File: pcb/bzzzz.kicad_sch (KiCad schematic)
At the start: 13 parts, among them J1 OUT, J2 OUT, Q1 FDD8424H

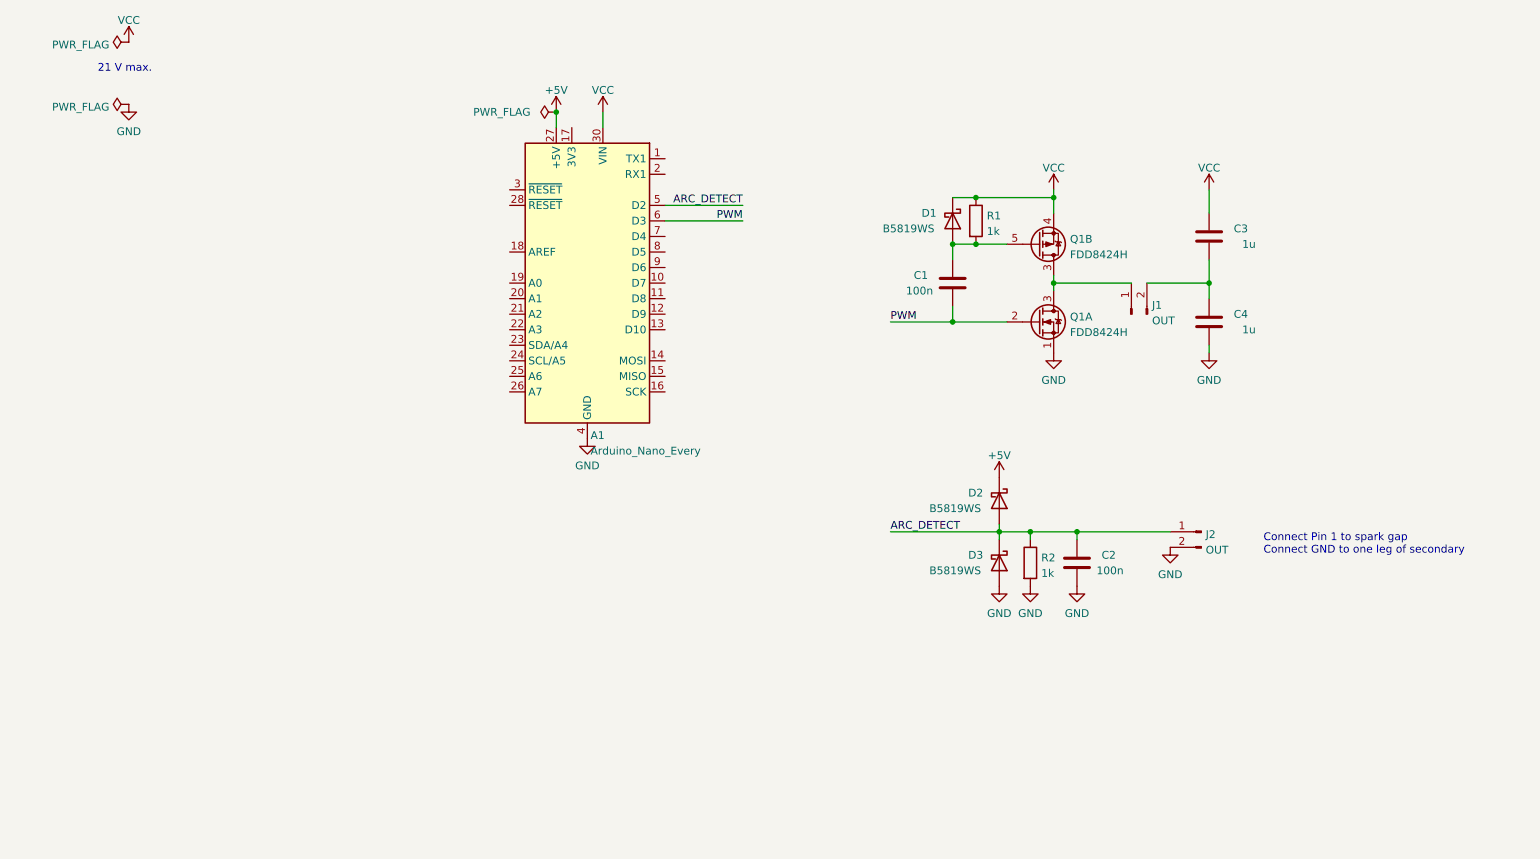
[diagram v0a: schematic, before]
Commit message: pcb: routing finished of a nice symmetric full-bridge
PCB fits below Arduino
Still need to choose smaller connectors
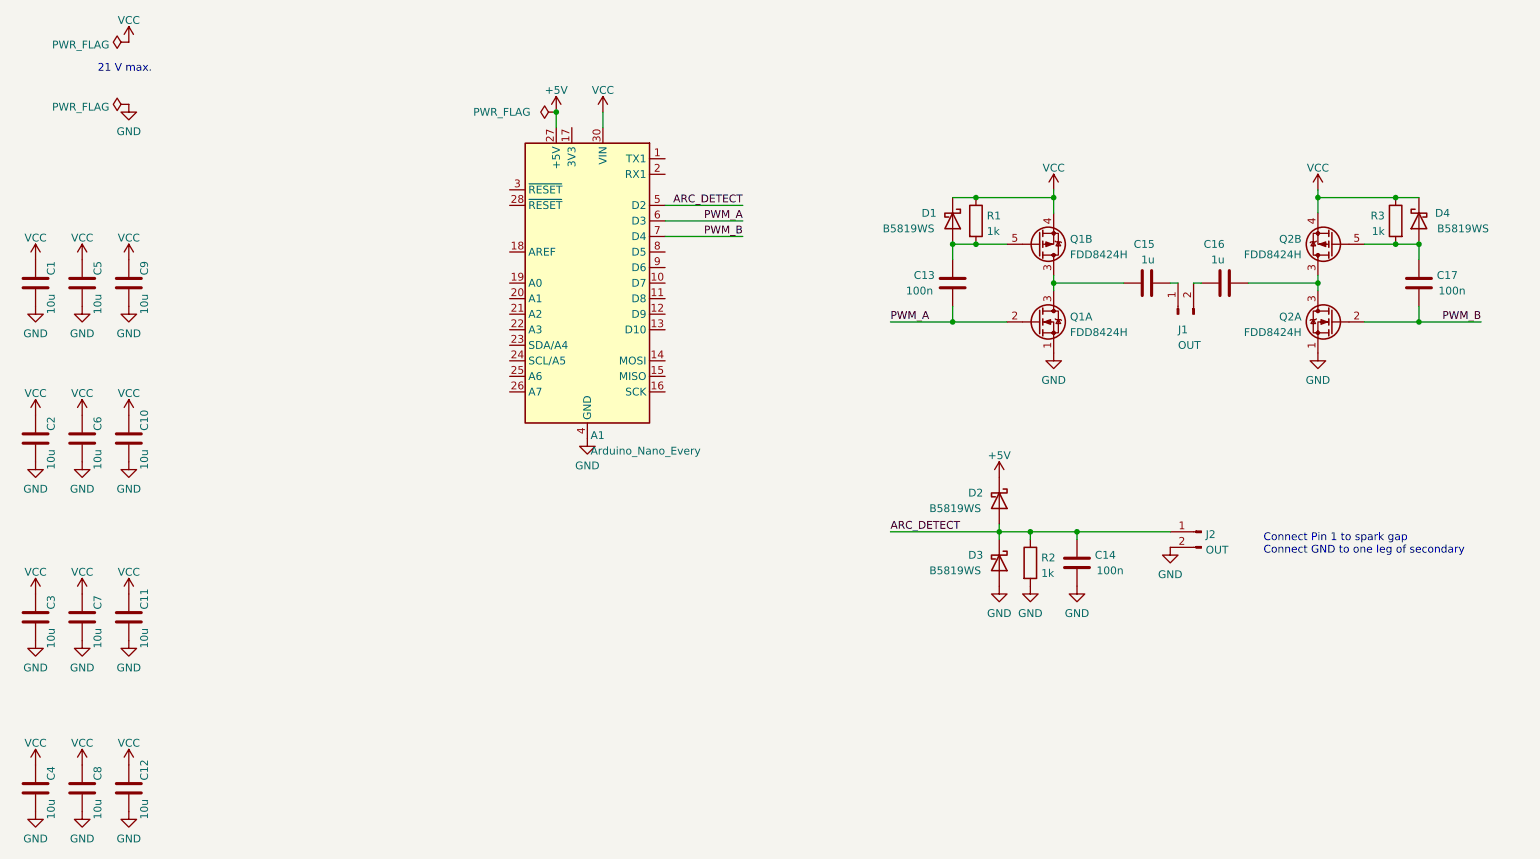
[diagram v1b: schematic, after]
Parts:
- added C1, C10, C11, C12, C2, C3, C5, C6, C7, C8, C9: 10u, Capacitor_SMD:C_0805_2012Metric, symbol Device:C
- added C16: 1u, Capacitor_SMD:C_1812_4532Metric, symbol Device:C
- added C17: 100n, Capacitor_SMD:C_0805_2012Metric, symbol Device:C
- added D4: B5819WS, Diode_SMD:D_SOD-323_HandSoldering, symbol Device:D_Schottky
- added Q2: FDD8424H, Package_TO_SOT_SMD:TO-252-4, symbol bzzzzz:FDD8424H
- added R3: 1k, Resistor_SMD:R_0805_2012Metric, symbol Device:R
- C15: renamed from C3; footprint Capacitor_SMD:C_0805_2012Metric -> Capacitor_SMD:C_1812_4532Metric
- C4: value 1u -> 10u
- renumbered C1 to C13, C2 to C14
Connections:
- net GND: now also C1.2, C10.2, C11.2, C12.2, C2.2, C3.2, C5.2, C6.2, C7.2, C8.2, C9.2, Q2.1 (S)
- net VCC: now also C4.1, C1.1, C10.1, C11.1, C12.1, C2.1, C3.1, C5.1, C6.1, C7.1, C8.1, C9.1, D4.1 (K), Q2.4 (S), R3.1; no longer C15.1
- net at Q1.3 (D), Q1.3 (D): now also C15.1; no longer J1.1 (Pin_1)
- net PWM_B: now reaches A1.7 (D4)
- net PWM_B: now also C17.2, Q2.2 (G)
- net PWM renamed PWM_A
- new net: C15.2, J1.1 (Pin_1)
- new net: C16.1, J1.2 (Pin_2)
- new net: C16.2, Q2.3 (D), Q2.3 (D)
- new net: C17.1, D4.2 (A), Q2.5 (G), R3.2
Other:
- moved on the sheet: C15, J1

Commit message: pcb ordered from jlc
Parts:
- added J1: PWR, Connector_PinHeader_2.54mm:PinHeader_1x02_P2.54mm_Horizontal, symbol Connector:Conn_01x02_Male
- J3: renamed from J2; value OUT -> ARC
- renumbered J1 to J2
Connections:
- net ARC_DETECT: now also A1.11 (D8); no longer A1.5 (D2)
- net GND: now also J1.2 (Pin_2)
- net PWM_A: now also A1.9 (D6); no longer A1.6 (D3)
- net PWM_B: now also A1.12 (D9); no longer A1.7 (D4)
- net VCC: now also J1.1 (Pin_1)
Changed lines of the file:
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@@
   (junction (at 194.31 124.46) (diameter 0) (color 0 0 0 0)
   )
+  (junction (at 52.07 54.61) (diameter 0) (color 0 0 0 0)
+  )
+  (junction (at 52.07 44.45) (diameter 0) (color 0 0 0 0)
+  )
   (junction (at 207.01 124.46) (diameter 0) (color 0 0 0 0)
   )
@@
     (stroke (width 0) (type default) (color 0 0 0 0))
   )
-  (wire (pts (xy 139.7 76.2) (xy 152.4 76.2))
+  (wire (pts (xy 139.7 88.9) (xy 152.4 88.9))
     (stroke (width 0) (type default) (color 0 0 0 0))
   )
@@
     (stroke (width 0) (type default) (color 0 0 0 0))
   )
+  (wire (pts (xy 52.07 50.8) (xy 52.07 54.61))
+    (stroke (width 0) (type default) (color 0 0 0 0))
+  )
   (wire (pts (xy 199.39 124.46) (xy 207.01 124.46))
     (stroke (width 0) (type default) (color 0 0 0 0))
@@
     (stroke (width 0) (type default) (color 0 0 0 0))
   )
+  (wire (pts (xy 52.07 44.45) (xy 52.07 48.26))
+    (stroke (width 0) (type default) (color 0 0 0 0))
+  )
   (wire (pts (xy 246.38 83.82) (xy 246.38 85.09))
     (stroke (width 0) (type default) (color 0 0 0 0))
@@
     (stroke (width 0) (type default) (color 0 0 0 0))
   )
-  (wire (pts (xy 152.4 71.12) (xy 139.7 71.12))
+  (wire (pts (xy 152.4 86.36) (xy 139.7 86.36))
     (stroke (width 0) (type default) (color 0 0 0 0))
   )
@@
     (stroke (width 0) (type default) (color 0 0 0 0))
   )
-  (wire (pts (xy 139.7 73.66) (xy 152.4 73.66))
+  (wire (pts (xy 139.7 81.28) (xy 152.4 81.28))
     (stroke (width 0) (type default) (color 0 0 0 0))
   )
@@
     (effects (font (size 1.27 1.27)) (justify left bottom))
   )
-  (text "21 V max." (at 46.99 49.53 0)
+  (text "21 V max." (at 33.02 49.53 0)
     (effects (font (size 1.27 1.27)) (justify left bottom))
   )
@@
     (effects (font (size 1.27 1.27)) (justify left bottom))
   )
-  (label "PWM_A" (at 152.4 73.66 180)
+  (label "PWM_A" (at 152.4 81.28 180)
     (effects (font (size 1.27 1.27)) (justify right bottom))
   )
@@
     (effects (font (size 1.27 1.27)) (justify left bottom))
   )
-  (label "ARC_DETECT" (at 152.4 71.12 180)
+  (label "ARC_DETECT" (at 152.4 86.36 180)
     (effects (font (size 1.27 1.27)) (justify right bottom))
   )
-  (label "PWM_B" (at 152.4 76.2 180)
+  (label "PWM_B" (at 152.4 88.9 180)
     (effects (font (size 1.27 1.27)) (justify right bottom))
   )
@@
   (symbol (lib_id "Connector:Conn_01x02_Male") (at 223.52 88.9 90) (unit 1)
     (in_bom yes) (on_board yes)
-    (property "Reference" "J1" (id 0) (at 223.52 91.44 90)
+    (property "Reference" "J2" (id 0) (at 223.52 91.44 90)
       (effects (font (size 1.27 1.27)) (justify right))
     )
@@
   (symbol (lib_id "Connector:Conn_01x02_Male") (at 227.33 124.46 0) (mirror y) (unit 1)
     (in_bom yes) (on_board yes) (fields_autoplaced)
-    (property "Reference" "J2" (id 0) (at 228.0412 124.8953 0)
+    (property "Reference" "J3" (id 0) (at 228.0412 124.8953 0)
       (effects (font (size 1.27 1.27)) (justify right))
     )
-    (property "Value" "OUT" (id 1) (at 228.0412 127.4322 0)
+    (property "Value" "ARC" (id 1) (at 228.0412 127.4322 0)
       (effects (font (size 1.27 1.27)) (justify right))
     )
@@
     (pin "2")
   )
+  (symbol (lib_id "Connector:Conn_01x02_Male") (at 46.99 48.26 0) (unit 1)
+    (in_bom yes) (on_board yes)
+    (property "Reference" "J1" (id 0) (at 55.88 45.72 0))
+    (property "Value" "PWR" (id 1) (at 55.88 49.53 0))
+    (property "Footprint" "Connector_PinHeader_2.54mm:PinHeader_1x02_P2.54mm_Horizontal" (id 2) (at 46.99 48.26 0)
+      (effects (font (size 1.27 1.27)) hide)
+    )
+    (property "Datasheet" "~" (id 3) (at 46.99 48.26 0)
+      (effects (font (size 1.27 1.27)) hide)
+    )
+    (pin "1")
+    (pin "2")
+  )
   (symbol (lib_id "power:VCC") (at 203.2 68.58 0) (unit 1)
     (in_bom yes) (on_board yes) (fields_autoplaced)
@@
       (reference "D4") (unit 1) (value "B5819WS") (footprint "Diode_SMD:D_SOD-323_HandSoldering")
     )
+    (path "/cb8eda5c-2aef-43d4-9df7-d3a6e27ad2af"
+      (reference "J1") (unit 1) (value "PWR") (footprint "Connector_PinHeader_2.54mm:PinHeader_1x02_P2.54mm_Horizontal")
+    )
     (path "/19063b58-7547-415c-b3a9-0c7e9916e739"
-      (reference "J1") (unit 1) (value "OUT") (footprint "Connector_PinHeader_2.54mm:PinHeader_1x02_P2.54mm_Horizontal")
+      (reference "J2") (unit 1) (value "OUT") (footprint "Connector_PinHeader_2.54mm:PinHeader_1x02_P2.54mm_Horizontal")
     )
     (path "/882a7cbb-fc6d-4b36-b1e2-ebe970cd2050"
-      (reference "J2") (unit 1) (value "OUT") (footprint "Connector_PinHeader_2.54mm:PinHeader_1x02_P2.54mm_Horizontal")
+      (reference "J3") (unit 1) (value "ARC") (footprint "Connector_PinHeader_2.54mm:PinHeader_1x02_P2.54mm_Horizontal")
     )
     (path "/03d96889-13d3-4cc5-8bb5-5866ad5abe7e"
